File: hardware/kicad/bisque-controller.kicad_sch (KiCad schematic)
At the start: 0 parts

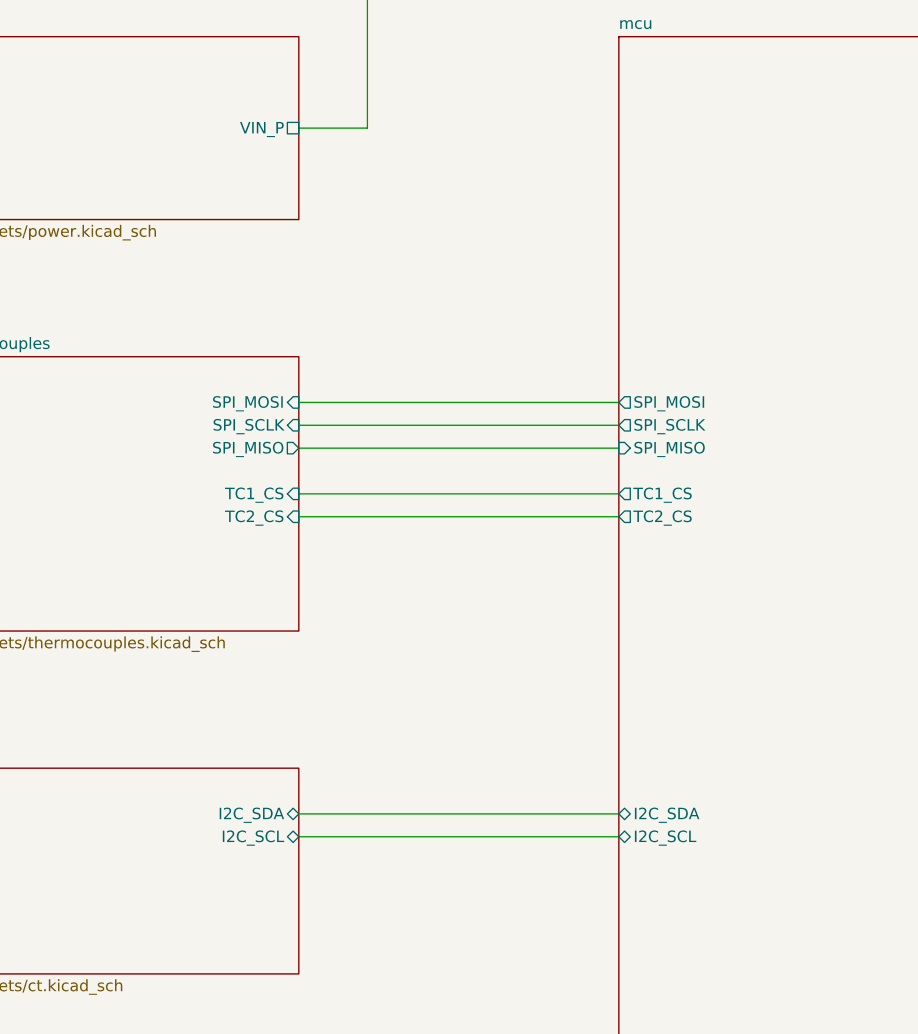
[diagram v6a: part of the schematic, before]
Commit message: hardware: the five quick fixes from the 2026-10-05/10-22 reviews
Schematic (rev B.3, sheets ct/power/mcu/ssr + root):
- R65, 1k from CTA_P to GND, mirrors R33 so the floating CT secondary
  sits at +-V/2 on IAP/IAN and channel A's pin limit is 139 A nominal,
  the same as channel B (schematic review 10-05 item 2).
- D9/D10 freewheel diodes are B5819W (JSCJ C8598, Basic, 1 A / 40 V,
  9 A surge) in the same SOD-123 land, replacing the 1N4148W whose
  150 mA rating never covered a 200 mA contactor coil (PCB review 10-05
  item 12). The SS34 was tried first and does not fit the SSR column.
- ADE_RESET is a hierarchical net to U1 IO37, the spare GPIO; the R30/C37
  RC stays for the power-on stretch (10-22 review E3).
- PWR_STATUS: BUCK_5V through R66 (100k) over R67+R68 (130k) to U1 IO45,
  2.8 V when the 24 V buck runs and 0 V on USB only (10-22 review E4).
  The TPS2116 ST pin would have said the same thing but its pad is boxed
  in by the USB pair on this layout, so it stays unconnected (C3, rev C).

Board:
- Every +5V layer transition (7) now has a second 0.6/0.3 via 0.85 mm
  away with a stub on each layer; the two in the USB corner use 0.3 mm
  stubs (fab-readiness C, "attempted, not landed" -> fixed).
- R65 placed below the CT filters; the divider in the two free columns
  south of U1, lifted 0.75 mm so the nameplate pocket keeps its 16.2 mm
  (it prints at 62% now). BUCK_5V tap hand-routed, the rest by the
  in-house router. DRC 0, make pcb-check ALL CHECKS PASS, 3D re-rendered.

Firmware/docs: KILN_PIN_ADE_RESET (37) and KILN_PIN_PWR_STATUS (45) in
Kconfig with the GPIO45 strapping caveat, check_pinmap NET_KCONFIG,
docs/pin-assignments.md (all 30 GPIOs assigned), DESIGN-NOTES sections
for each change, status notes in the four review documents, gen_jlc
sourcing + JLC_PLACEMENT rows, lcsc_pads cache and datasheet manifest.

Co-Authored-By: Claude Fable 5.1 <noreply@anthropic.com>
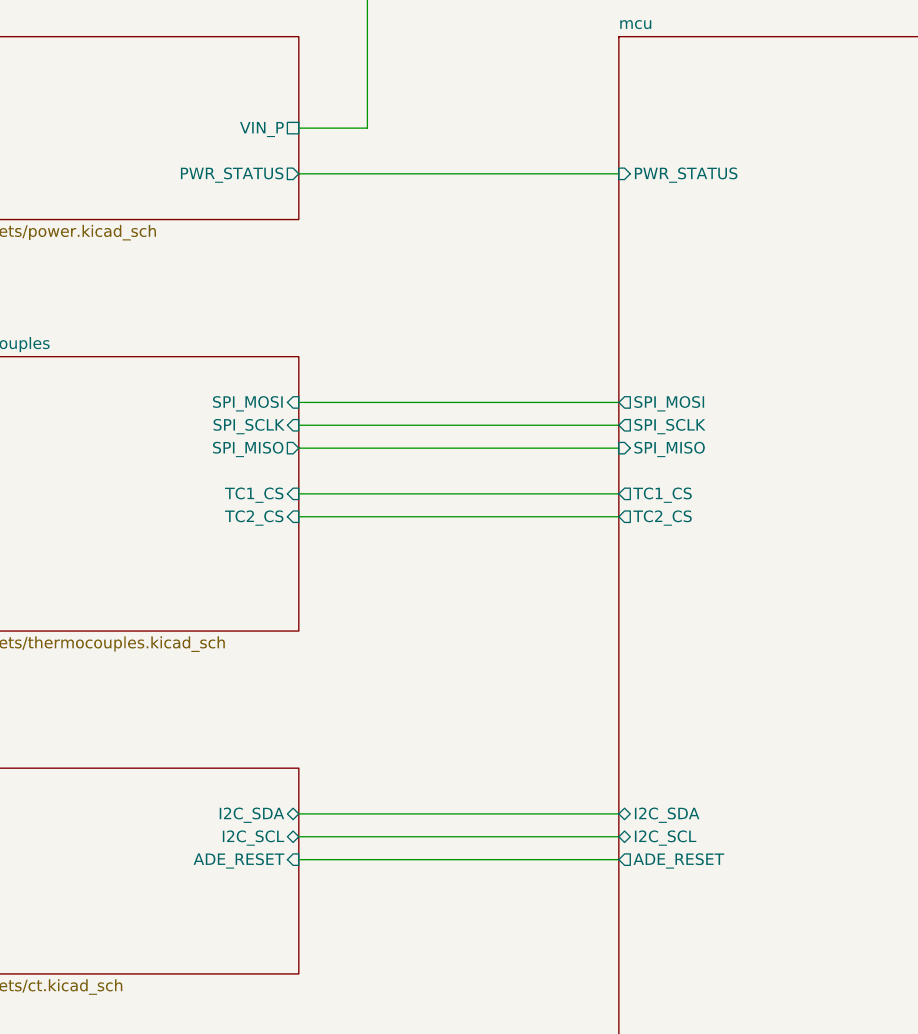
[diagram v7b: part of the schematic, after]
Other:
- sheet ct ports: added ADE_RESET; removed none
- sheet mcu ports: added ADE_RESET, PWR_STATUS; removed none
- sheet power ports: added PWR_STATUS; removed none
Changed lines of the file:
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@@
 		(comment 2 "4-layer, 100 x 100 mm, JLCPCB standard process")
 	)
+	(wire
+		(pts
+			(xy 139.7 33.02)
+			(xy 154.94 33.02)
+		)
+		(stroke
+			(width 0)
+			(type default)
+		)
+	)
+	(wire
+		(pts
+			(xy 58.42 63.5)
+			(xy 93.98 63.5)
+		)
+		(stroke
+			(width 0)
+			(type default)
+		)
+	)
+	(wire
+		(pts
+			(xy 66.04 15.24)
+			(xy 165.1 15.24)
+		)
+		(stroke
+			(width 0)
+			(type default)
+		)
+	)
+	(wire
+		(pts
+			(xy 58.42 71.12)
+			(xy 93.98 71.12)
+		)
+		(stroke
+			(width 0)
+			(type default)
+		)
+	)
+	(wire
+		(pts
+			(xy 58.42 106.68)
+			(xy 93.98 106.68)
+		)
+		(stroke
+			(width 0)
+			(type default)
+		)
+	)
+	(wire
+		(pts
+			(xy 139.7 68.58)
+			(xy 154.94 68.58)
+		)
+		(stroke
+			(width 0)
+			(type default)
+		)
+	)
+	(wire
+		(pts
+			(xy 139.7 35.56)
+			(xy 154.94 35.56)
+		)
+		(stroke
+			(width 0)
+			(type default)
+		)
+	)
+	(wire
+		(pts
+			(xy 66.04 30.48)
+			(xy 66.04 15.24)
+		)
+		(stroke
+			(width 0)
+			(type default)
+		)
+	)
+	(wire
+		(pts
+			(xy 58.42 60.96)
+			(xy 93.98 60.96)
+		)
+		(stroke
+			(width 0)
+			(type default)
+		)
+	)
+	(wire
+		(pts
+			(xy 139.7 76.2)
+			(xy 154.94 76.2)
+		)
+		(stroke
+			(width 0)
+			(type default)
+		)
+	)
+	(wire
+		(pts
+			(xy 58.42 66.04)
+			(xy 93.98 66.04)
+		)
+		(stroke
+			(width 0)
+			(type default)
+		)
+	)
+	(wire
+		(pts
+			(xy 139.7 73.66)
+			(xy 154.94 73.66)
+		)
+		(stroke
+			(width 0)
+			(type default)
+		)
+	)
+	(wire
+		(pts
+			(xy 139.7 78.74)
+			(xy 154.94 78.74)
+		)
+		(stroke
+			(width 0)
+			(type default)
+		)
+	)
+	(wire
+		(pts
+			(xy 139.7 66.04)
+			(xy 154.94 66.04)
+		)
+		(stroke
+			(width 0)
+			(type default)
+		)
+	)
+	(wire
+		(pts
+			(xy 139.7 30.48)
+			(xy 154.94 30.48)
+		)
+		(stroke
+			(width 0)
+			(type default)
+		)
+	)
+	(wire
+		(pts
+			(xy 58.42 73.66)
+			(xy 93.98 73.66)
+		)
+		(stroke
+			(width 0)
+			(type default)
+		)
+	)
+	(wire
+		(pts
+			(xy 139.7 63.5)
+			(xy 154.94 63.5)
+		)
+		(stroke
+			(width 0)
+			(type default)
+		)
+	)
+	(wire
+		(pts
+			(xy 165.1 15.24)
+			(xy 165.1 20.32)
+		)
+		(stroke
+			(width 0)
+			(type default)
+		)
+	)
+	(wire
+		(pts
+			(xy 58.42 109.22)
+			(xy 93.98 109.22)
+		)
+		(stroke
+			(width 0)
+			(type default)
+		)
+	)
+	(wire
+		(pts
+			(xy 58.42 30.48)
+			(xy 66.04 30.48)
+		)
+		(stroke
+			(width 0)
+			(type default)
+		)
+	)
+	(wire
+		(pts
+			(xy 139.7 60.96)
+			(xy 154.94 60.96)
+		)
+		(stroke
+			(width 0)
+			(type default)
+		)
+	)
+	(wire
+		(pts
+			(xy 58.42 111.76)
+			(xy 93.98 111.76)
+		)
+	)
+	(wire
+		(pts
+			(xy 58.42 35.56)
+			(xy 93.98 35.56)
+		)
+	)
 	(text "NOTES  -  Bisque kiln controller, rev B"
-		(exclude_from_sim no)
 		(at 199.8 27.7 0)
 		(effects
@@
 	)
 	(text "SSR terminals J4/J9: pin1 = VIN_P (24 V, fused and TVS-clamped,\n  ALWAYS LIVE), pin2 = the switched low side. The watchdog gates\n  the shared return (Q7), not the supply, so a tripped watchdog\n  leaves 24 V on pin 1 and opens pin 2. Boot-safe: R7/R20 hold\n  each gate down while the optos are dark.\n  The optos are NOT an isolation barrier - both sides share GND.\n  Rev B's opto-ISOLATED design was reverted and stays reverted;\n  U8/U9 are here to keep a 24 V gate fault off the GPIO.\n  Per channel <=200 mA: F1 holds at 750 mA and U11 takes ~250.\n\nTC1 terminal J3 / TC2 terminal J8: pin1 = K+, pin2 = K- - both\n  float, biased near AGND only through each MAX31856's internal\n  BIAS network. Ungrounded-junction probes required: two\n  grounded-junction probes in one kiln would loop through it.\n\nNav switch J6 is panel-mounted; inputs use ESP32 pull-ups.\n\nJ11: IN1/IN2/IN3 (lid/gas-flow/spare) + GND - dry contact each\n  channel to GND.\n\nDisplay J5 (14-pin, ST7796S + XPT2046 touch module, LCDWIKI\n  MSP4021): 1=+5V 2=GND 3=CS 4=RST 5=DC 6=SDI/MOSI 7=SCK 8=BL\n  9=SDO/MISO 10=T_CLK 11=T_CS 12=T_DIN 13=T_DO 14=T_IRQ.\n  PIN 1 IS +5V, NOT 3V3 - the module regulates on board; do not\n  wire a 3.3V-only panel to it. Logic is 3.3V; touch shares SPI2\n  with the LCD and both MAX31856s (R39-R43 damping). LCD_RST is\n  GPIO46, a boot-strapping pin: the MSP4021 has NO pull-up on its\n  RESET line (QDtech schematic, 2019-09-27), so download mode is\n  unaffected - check that before substituting another module.\n\nJ12: CT current inputs, CTA_P/CTA_N/CTB_P/CTB_N - one CT clamp\n  per SSR zone.\n\nJ13: DNP SELV voltage sense header. NOT mains-rated, not fitted\n  - do not wire to AC mains. Y1 is a packaged 3.579545 MHz\n  oscillator (no load caps; C25 is its bypass) - see\n  DESIGN-NOTES.md, Y1. ADE7953 I2C address 0x38 would collide\n  with a PCF8574A added on J7/J14.\n\nDesign reasoning per block: hardware/kicad/DESIGN-NOTES.md.\nDesignators C8, C9, C26, D1, D2 and Q1 are retired, not missing:\n  they are kept free so the notes and reviews still read."
-		(exclude_from_sim no)
 		(at 199.8 86.36 0)
 		(effects
@@
 			)
 			(justify left)
-		)
-	)
-	(wire
-		(pts
-			(xy 139.7 33.02) (xy 154.94 33.02)
-		)
-		(stroke
-			(width 0)
-			(type default)
-		)
-	)
-	(wire
-		(pts
-			(xy 58.42 63.5) (xy 93.98 63.5)
-		)
-		(stroke
-			(width 0)
-			(type default)
-		)
-	)
-	(wire
-		(pts
-			(xy 66.04 15.24) (xy 165.1 15.24)
-		)
-		(stroke
-			(width 0)
-			(type default)
-		)
-	)
-	(wire
-		(pts
-			(xy 58.42 71.12) (xy 93.98 71.12)
-		)
-		(stroke
-			(width 0)
-			(type default)
-		)
-	)
-	(wire
-		(pts
-			(xy 58.42 106.68) (xy 93.98 106.68)
-		)
-		(stroke
-			(width 0)
-			(type default)
-		)
-	)
-	(wire
-		(pts
-			(xy 139.7 68.58) (xy 154.94 68.58)
-		)
-		(stroke
-			(width 0)
-			(type default)
-		)
-	)
-	(wire
-		(pts
-			(xy 139.7 35.56) (xy 154.94 35.56)
-		)
-		(stroke
-			(width 0)
-			(type default)
-		)
-	)
-	(wire
-		(pts
-			(xy 66.04 30.48) (xy 66.04 15.24)
-		)
-		(stroke
-			(width 0)
-			(type default)
-		)
-	)
-	(wire
-		(pts
-			(xy 58.42 60.96) (xy 93.98 60.96)
-		)
-		(stroke
-			(width 0)
-			(type default)
-		)
-	)
-	(wire
-		(pts
-			(xy 139.7 76.2) (xy 154.94 76.2)
-		)
-		(stroke
-			(width 0)
-			(type default)
-		)
-	)
-	(wire
-		(pts
-			(xy 58.42 66.04) (xy 93.98 66.04)
-		)
-		(stroke
-			(width 0)
-			(type default)
-		)
-	)
-	(wire
-		(pts
-			(xy 139.7 73.66) (xy 154.94 73.66)
-		)
-		(stroke
-			(width 0)
-			(type default)
-		)
-	)
-	(wire
-		(pts
-			(xy 139.7 78.74) (xy 154.94 78.74)
-		)
-		(stroke
-			(width 0)
-			(type default)
-		)
-	)
-	(wire
-		(pts
-			(xy 139.7 66.04) (xy 154.94 66.04)
-		)
-		(stroke
-			(width 0)
-			(type default)
-		)
-	)
-	(wire
-		(pts
-			(xy 139.7 30.48) (xy 154.94 30.48)
-		)
-		(stroke
-			(width 0)
-			(type default)
-		)
-	)
-	(wire
-		(pts
-			(xy 58.42 73.66) (xy 93.98 73.66)
-		)
-		(stroke
-			(width 0)
-			(type default)
-		)
-	)
-	(wire
-		(pts
-			(xy 139.7 63.5) (xy 154.94 63.5)
-		)
-		(stroke
-			(width 0)
-			(type default)
-		)
-	)
-	(wire
-		(pts
-			(xy 165.1 15.24) (xy 165.1 20.32)
-		)
-		(stroke
-			(width 0)
-			(type default)
-		)
-	)
-	(wire
-		(pts
-			(xy 58.42 109.22) (xy 93.98 109.22)
-		)
-		(stroke
-			(width 0)
-			(type default)
-		)
-	)
-	(wire
-		(pts
-			(xy 58.42 30.48) (xy 66.04 30.48)
-		)
-		(stroke
-			(width 0)
-			(type default)
-		)
-	)
-	(wire
-		(pts
-			(xy 139.7 60.96) (xy 154.94 60.96)
-		)
-		(stroke
-			(width 0)
-			(type default)
 		)
 	)
@@
 			)
 		)
+		(pin "ADE_RESET" output
+			(at 93.98 111.76 180)
+			(effects
+				(font
+					(size 1.27 1.27)
+				)
+				(justify left)
+			)
+		)
+		(pin "PWR_STATUS" input
+			(at 93.98 35.56 180)
+			(effects
+				(font
+					(size 1.27 1.27)
+				)
+				(justify left)
+			)
+		)
 		(instances
 			(project "bisque-controller"
@@
 			)
 		)
+		(pin "ADE_RESET" input
+			(at 58.42 111.76 0)
+			(effects
+				(font
+					(size 1.27 1.27)
+				)
+				(justify right)
+			)
+		)
 		(instances
 			(project "bisque-controller"
@@
 			(effects
 				(font
+					(size 1.27 1.27)
+				)
+				(justify right)
+			)
+		)
+		(pin "PWR_STATUS" output
+			(at 58.42 35.56 0)
+			(effects
+				(font
